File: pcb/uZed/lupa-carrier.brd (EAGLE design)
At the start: 99.7 x 57.1 mm, 93 parts, among them K1 694108105102

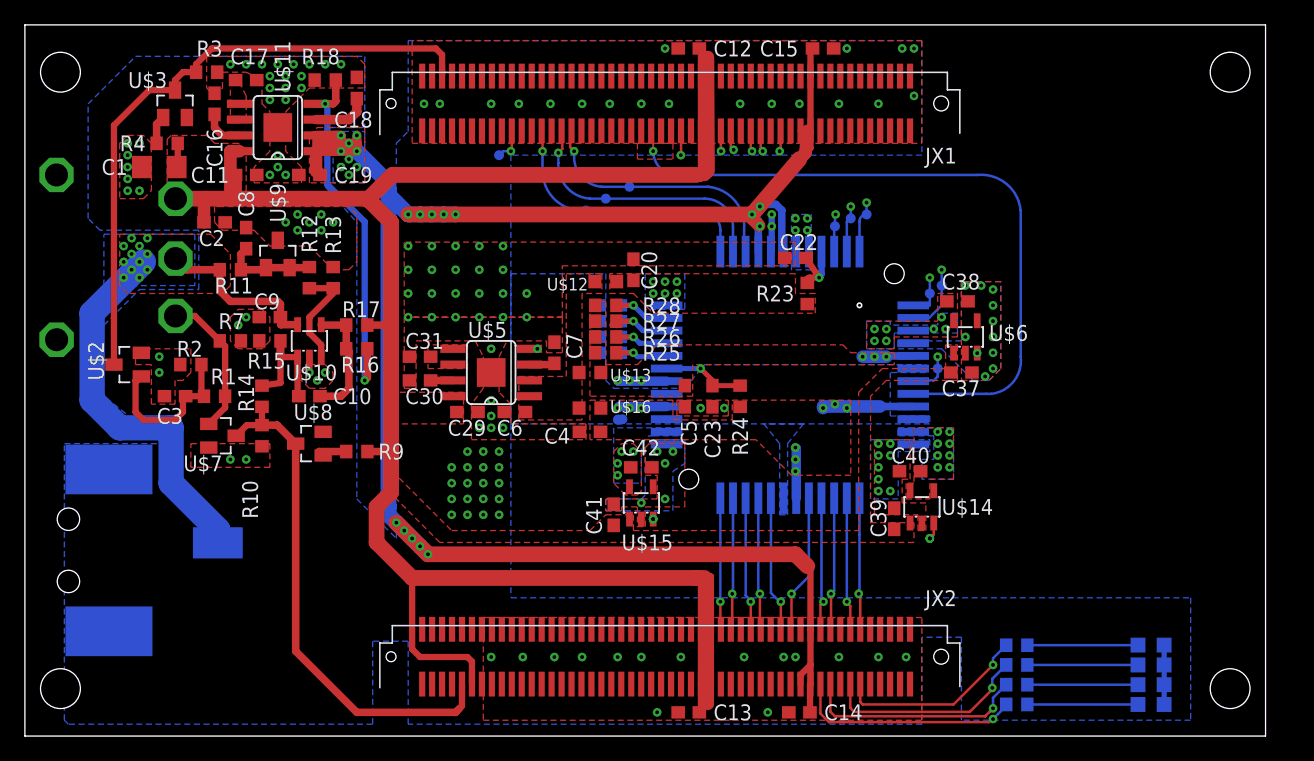
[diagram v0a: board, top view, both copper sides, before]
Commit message: added hdmi connectors, routing in progress
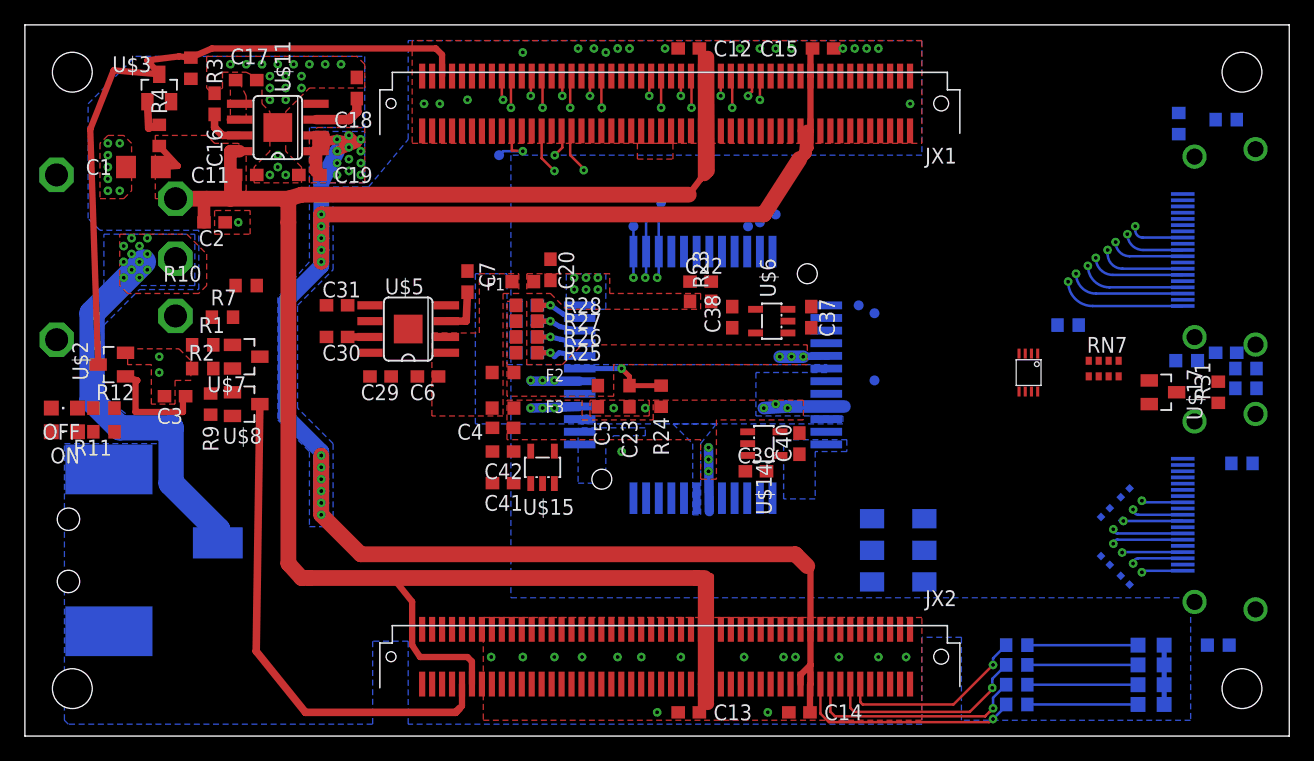
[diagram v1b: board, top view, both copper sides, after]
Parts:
- removed C10, C8, C9: .1uF, rcl:C0603
- removed R13, R14: 1k, rcl:R0603
- removed R15: 3k74, rcl:R0603
- removed R16: 0, rcl:R0603
- removed R17: 3k, rcl:R0603
- removed R18: 100k, rcl:R0603
- removed U$10: AP331A, lupa300-components:SOT25
- removed U$12, U$13, U$16: BLM18, lupa300-components:C0603K
- removed U$9: TL431A, lupa300-components:SOT23
- added C21, C28: .1uF, rcl:C0603K
- added C32: (no value), rcl:C0603
- added F1, F2, F3: BLM18, lupa300-components:C0603K
- added J5, J6: HDMI-TYPE-A-RECEPTICALFCI10029449, saanlima:FCI-HDMI-TYPE-A-RECEPT
- added OFF, ON: (no value), adafruit:CHIPLED_0805
- added PCA9306: PCA9306, saanlima:PSOP-8
- added R21, R8: 100K, rcl:R0603
- added R22, R32: 0, rcl:R0603
- added R29, R30, R31: 10K, rcl:R0603
- added RN3, RN4, RN5, RN6: 51, resistor-dil:EXB34V
- added RN7: 2k, resistor-dil:0603-ARV
- added U$17: BSS138, lupa300-components:SOT23
- added U$18: SI514, lupa300-components:XTAL-6PIN
- R12: value 1k5 -> 1k
- moved R12 19.6 mm to (6.35, 26.4), turned to 0 degrees
- moved C38 18.1 mm to (56.8, 33.7), turned to 90 degrees
- moved R11 16.5 mm to (6.35, 24.4), turned to 180 degrees
- moved U$6 15.6 mm to (60.0, 33.3), turned to 90 degrees
- moved U$14 13.7 mm to (59.4, 23.5), turned to 270 degrees
- moved C37 12.9 mm to (63.2, 33.7), turned to 90 degrees
- moved R9 12.3 mm to (14.9, 26.7), turned to 270 degrees
- moved R10 12.1 mm to (17.8, 36.2), turned to 180 degrees
- moved C39 11.7 mm to (58.7, 21.3), turned to 0 degrees
- moved C42 11.2 mm to (38.4, 22.9), turned to 180 degrees
- moved C41 9.25 mm to (38.4, 20.3), turned to 180 degrees
- moved C40 9.16 mm to (62.2, 23.5), turned to 270 degrees
- moved C7 9.03 mm to (35.6, 36.5)
- moved R23 8.60 mm to (54.3, 34.9), turned to 180 degrees
- moved U$15 8.44 mm to (41.6, 21.6)
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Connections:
- removed net 2V5_REF: C8.1, R11.2, R12.1, U$9.1, U$9.2
- removed net N$7: C10.1, R14.2, R15.1, U$10.1
- removed net N$9: C10.2, R16.1, R17.1, U$10.4
- removed net VADJ_EN: R16.2, R18.2, U$11.4
- new net 3V3: C32.1, PCA9306.2, R22.2, R31.1, RN7.1, RN7.2, U$18.P$6
- new net DET_CONTROL: R31.2, U$17.1
- new net HDMI_OSC: JX2.P$47, U$18.P$4
- new net HDMI_PU: R22.1, RN3.3, RN3.4, RN4.3, RN4.4, RN5.3, RN5.4, RN6.3, RN6.4
- new net N$17: J5.19, R29.2
- new net N$18: J6.19, R30.1, U$17.3
- new net N$19: J6.16, PCA9306.5, RN7.5
- new net N$20: J6.15, PCA9306.6, RN7.6
- new net N$21: J5.18, R32.2
- new net N$24: OFF.A, R12.1
- new net N$34: C21.1, J6.SH1, J6.SH2, J6.SH3, J6.SH4, R8.2
- new net N$6: C28.1, J5.SH1, J5.SH2, J5.SH3, J5.SH4, R21.2
- new net P1_CLOCK+: J6.10, JX1.P$66, RN3.2
- new net P1_CLOCK-: J6.12, JX1.P$64, RN3.1
- new net P1_DATA0+: J6.7, JX1.P$72, RN4.2
- new net P1_DATA0-: J6.9, JX1.P$70, RN4.1
- new net P1_DATA1+: J6.4, JX1.P$78, RN5.2
- new net P1_DATA1-: J6.6, JX1.P$76, RN5.1
- new net P1_DATA2+: J6.1, JX1.P$84, RN6.2
- new net P1_DATA2-: J6.3, JX1.P$82, RN6.1
- new net P2_CLOCK+: J5.10, JX1.P$34
- new net P2_CLOCK-: J5.12, JX1.P$32
- new net P2_DATA0+: J5.7, JX1.P$40
- new net P2_DATA0-: J5.9, JX1.P$38
- new net P2_DATA1+: J5.4, JX1.P$48
- new net P2_DATA1-: J5.6, JX1.P$46
- new net P2_DATA2+: J5.1, JX1.P$54
- new net P2_DATA2-: J5.3, JX1.P$52
- new net SCL2: PCA9306.3, RN7.8
- new net SCLC: U$18.P$2
- new net SDA2: PCA9306.4, RN7.7
- new net SDAC: U$18.P$1
- net 5V: now also J6.18, PCA9306.7, PCA9306.8, R11.1, R30.2, R32.1, RN7.3, RN7.4; no longer R17.2
- net 5V_OFF: now also R12.2
- net GND: now also C21.2, C28.2, C32.2, J5.11, J5.14, J5.17, J5.2, J5.5, J5.8, J6.11, J6.14, J6.17, J6.2, J6.5, J6.8, OFF.C, ON.C, PCA9306.1, R21.1, R29.1, R8.1, U$17.2, U$18.P$3; no longer C8.2, C9.2, R13.1, R15.2, R18.1, U$10.2, U$9.3
- net N$2: now also F1.2, F2.2, F3.2; no longer U$12.2, U$13.2, U$16.2
- net N$5: now also ON.A, R11.2; no longer R12.2, R13.2, U$10.3
- net VADC: now also F3.1; no longer U$16.1
- net VCCIO_EN: now also U$11.4; no longer R14.1
- net VDDA: now also F2.1; no longer U$13.1
- net VIN: no longer C9.1, R11.1, U$10.5
- net VPIX: now also F1.1; no longer U$12.1
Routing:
- net LPOWEN: track 89.6 -> 4.49 mm, vias 7 -> 1
- net P1_DATA2+: track 0.00 -> 84.7 mm, vias 0 -> 2
- net P1_DATA2-: track 0.00 -> 84.2 mm, vias 0 -> 2
- net P1_DATA1+: track 0.00 -> 81.3 mm, vias 0 -> 2
- net P1_DATA1-: track 0.00 -> 80.5 mm, vias 0 -> 2
- net P1_DATA0+: track 0.00 -> 78.2 mm, vias 0 -> 2
- net P1_DATA0-: track 0.00 -> 77.6 mm, vias 0 -> 2
- net P1_CLOCK+: track 0.00 -> 75.3 mm, vias 0 -> 2
- net P1_CLOCK-: track 0.00 -> 74.1 mm, vias 0 -> 2
- net P2_DATA2+: track 0.00 -> 57.5 mm, vias 0 -> 2
- net P2_DATA2-: track 0.00 -> 55.5 mm, vias 0 -> 2
- net CLK: track 55.1 -> 0.23 mm, vias 1 -> 0
- net P2_DATA1+: track 0.00 -> 51.6 mm, vias 0 -> 2
- net P2_DATA1-: track 0.00 -> 50.3 mm, vias 0 -> 2
- net P2_DATA0+: track 0.00 -> 47.3 mm, vias 0 -> 2
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- removed copper zone on layer 1, net N$23
- removed copper zone on layer 1, net VDDD
- removed copper zone on layer 16, net VDDD
- removed copper zone on layer 1, net VDDD1
- removed copper zone on layer 1, net VDDO
- removed copper zone on layer 16, net VDDO
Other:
- board size 99.7 x 57.1 mm -> 101.6 x 57.1 mm

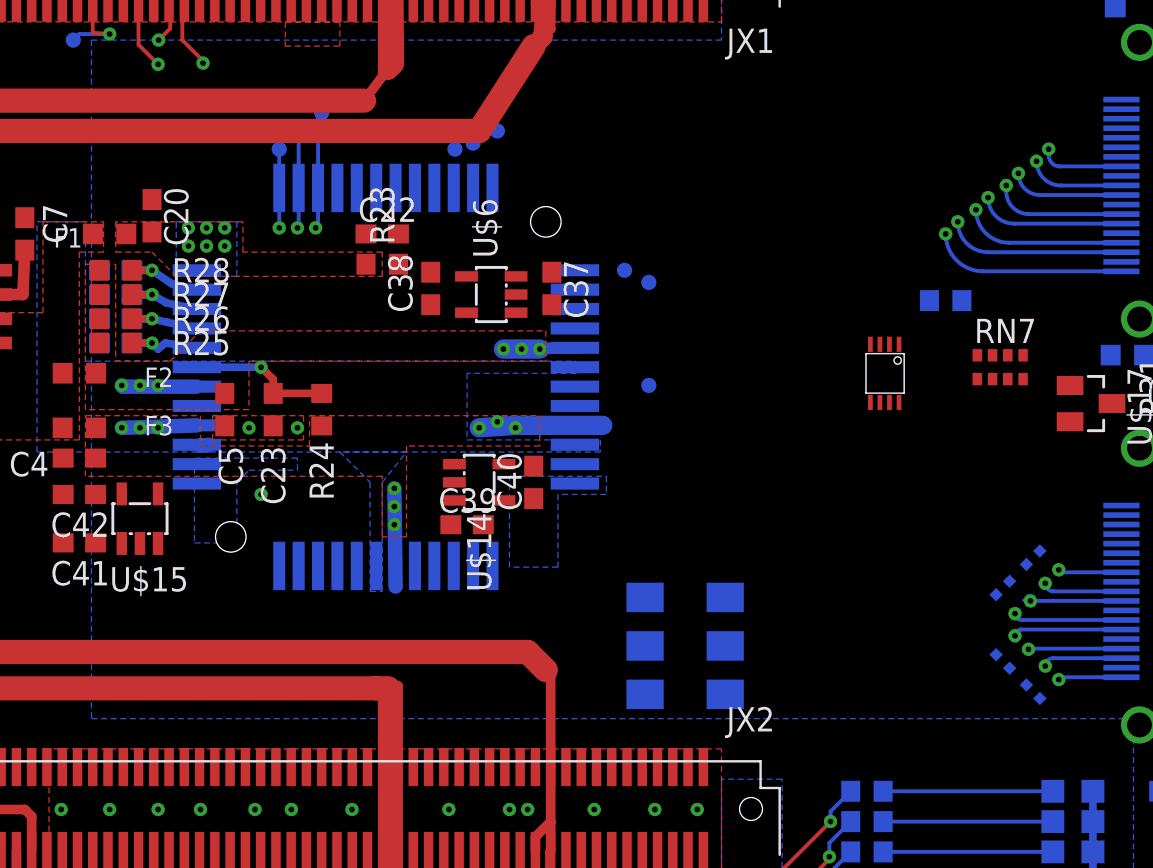
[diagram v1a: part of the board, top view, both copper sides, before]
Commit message: length tuned hdmi in traces
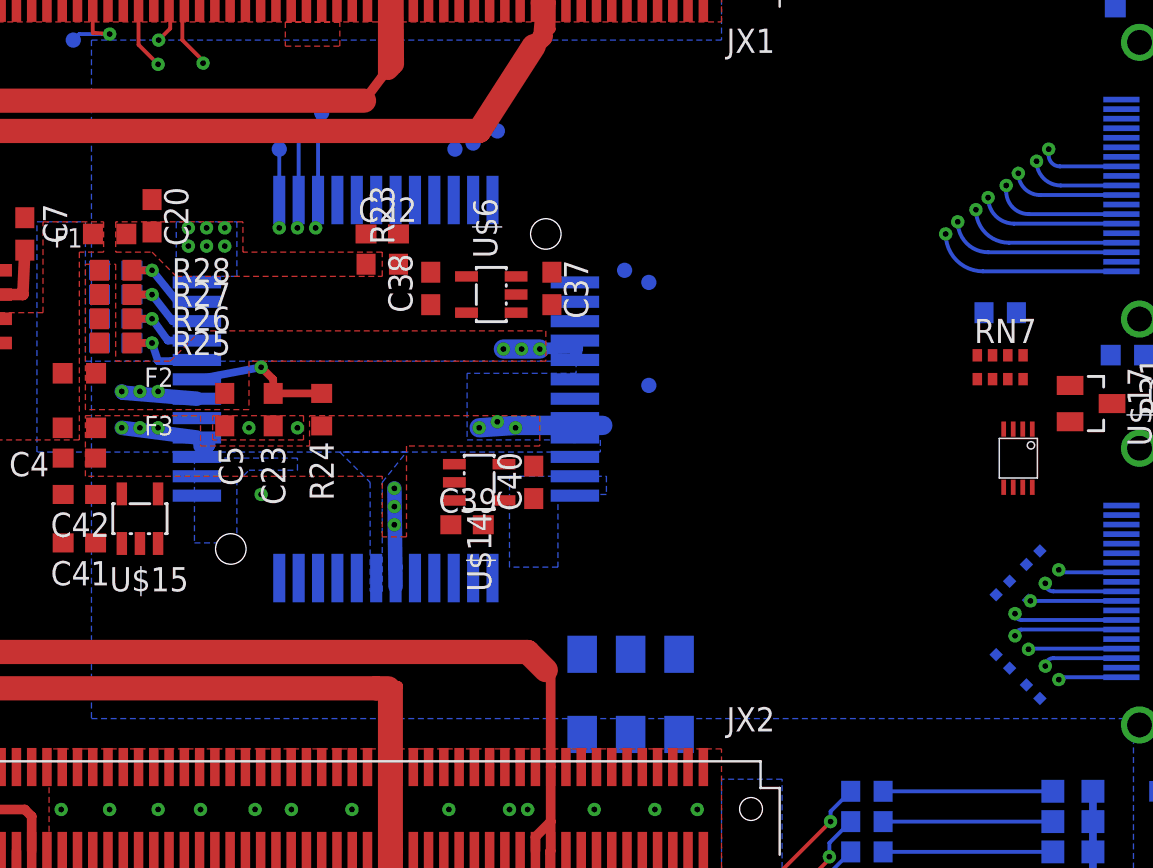
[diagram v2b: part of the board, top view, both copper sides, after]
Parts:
- moved PCA9306 8.28 mm to (87.6, 24.8)
- moved U$18 3.82 mm to (67.3, 12.4), turned to 90 degrees
- moved R22 2.93 mm to (86.7, 32.4)
- moved U$4 0.63 mm to (61.6, 21.3)
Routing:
- net P1_CLOCK-: track 74.1 -> 85.0 mm
- net P1_CLOCK+: track 75.3 -> 85.0 mm
- net P1_DATA0-: track 77.6 -> 84.6 mm
- net P1_DATA0+: track 78.2 -> 84.3 mm
- net P1_DATA1-: track 80.5 -> 84.1 mm
- net P1_DATA1+: track 81.3 -> 84.2 mm
- net VADC: track 17.2 -> 19.0 mm
- net P1_DATA2+: track 84.7 -> 85.4 mm
- net P1_DATA2-: track 84.2 -> 84.9 mm
- net BIAS1: track 4.71 -> 5.25 mm
- net VDDA: track 9.87 -> 10.4 mm
- net BIAS3: track 4.51 -> 5.04 mm
- net BIAS2: track 5.34 -> 5.87 mm

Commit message: length tuning
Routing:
- net P2_CLOCK-: track 45.4 -> 48.5 mm
- net P2_CLOCK+: track 47.2 -> 50.3 mm
- net P2_DATA0-: track 45.5 -> 48.2 mm
- net P2_DATA0+: track 47.3 -> 49.9 mm
- net P2_DATA2-: track 55.5 -> 58.1 mm
- net P2_DATA2+: track 57.5 -> 59.4 mm
- net P2_DATA1-: track 50.3 -> 51.9 mm
- net P2_DATA1+: track 51.6 -> 53.0 mm

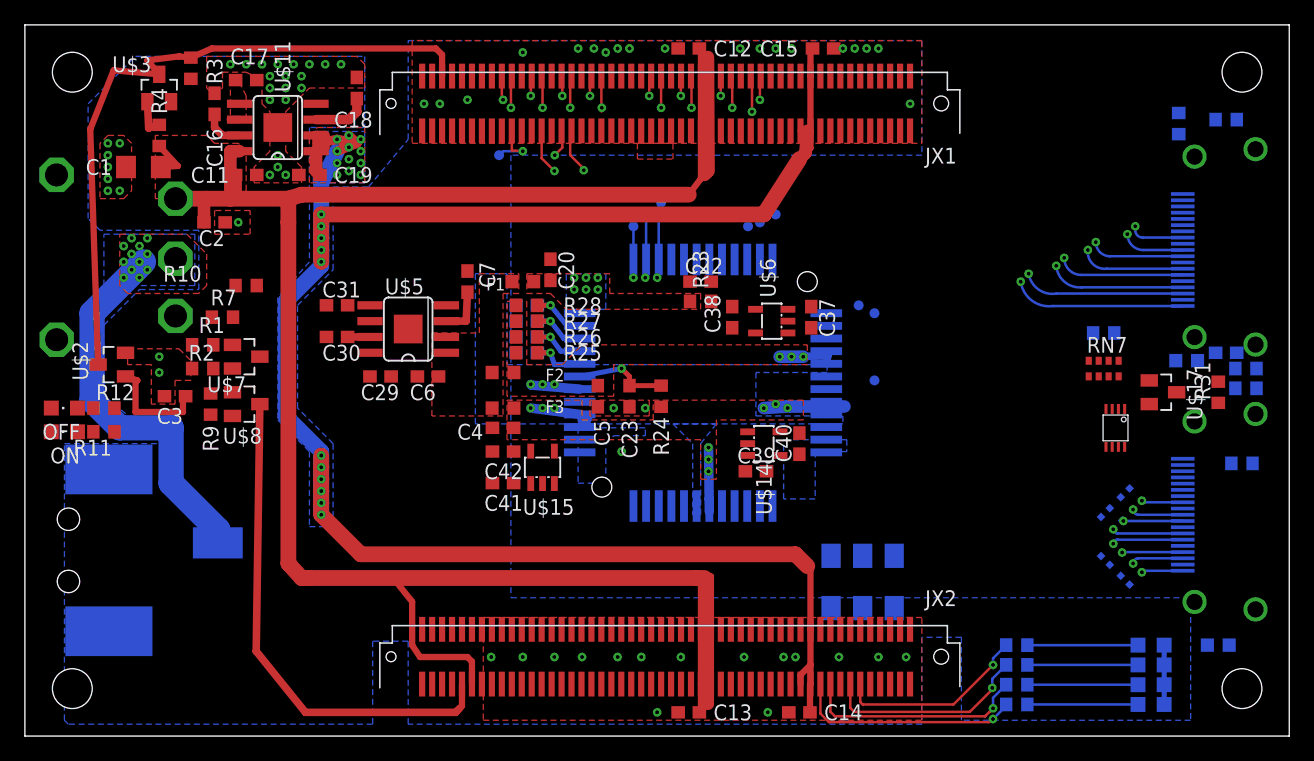
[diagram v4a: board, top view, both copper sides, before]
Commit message: beginning 4 layer hdmi board, discarded 6 layer approach
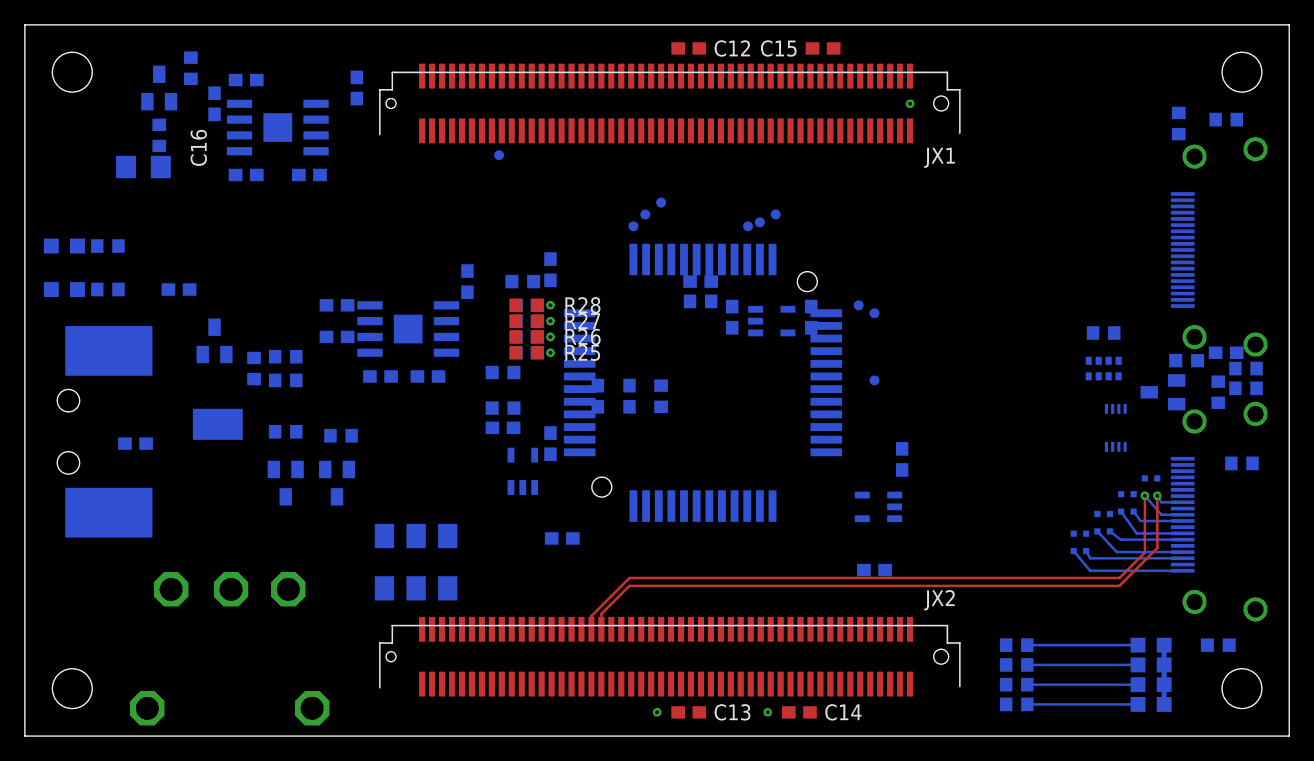
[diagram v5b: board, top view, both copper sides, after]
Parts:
- moved U$18 35.9 mm to (31.4, 14.0), turned to 270 degrees
- moved U$1 33.1 mm to (8.57, 13.7), turned to 180 degrees
- moved R12 13.0 mm to (6.67, 39.4), flipped to the bottom, turned to 180 degrees
- moved OFF 13.0 mm to (3.17, 39.4), flipped to the bottom, turned to 270 degrees
- moved C39 12.4 mm to (68.3, 13.3), flipped to the bottom
- moved R10 12.2 mm to (21.0, 24.4), flipped to the bottom
- moved R11 11.4 mm to (6.67, 35.9), flipped to the bottom, turned to 0 degrees
- moved ON 11.4 mm to (3.17, 35.9), flipped to the bottom, turned to 270 degrees
- moved R9 10.8 mm to (25.4, 24.1), flipped to the bottom, turned to 180 degrees
- moved U$7 10.6 mm to (21.0, 20.3), flipped to the bottom, turned to 180 degrees
- moved U$14 10.5 mm to (68.6, 18.4), flipped to the bottom
- moved U$8 9.68 mm to (25.1, 20.3), flipped to the bottom, turned to 180 degrees
- moved K1 9.53 mm to (0.00, 24.4)
- moved U$2 8.47 mm to (15.2, 31.8), flipped to the bottom, turned to 0 degrees
- moved C40 8.35 mm to (70.5, 22.2), flipped to the bottom
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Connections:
- net P1_CLOCK+: now also JX2.P$66
- net P1_CLOCK-: now also JX2.P$64
- net P1_DATA0+: now also JX2.P$72
- net P1_DATA0-: now also JX2.P$70
- net P1_DATA1+: now also JX2.P$78
- net P1_DATA1-: now also JX2.P$76
- net P1_DATA2+: now also JX2.P$84
- net P1_DATA2-: now also JX2.P$82
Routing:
- net 5V: track 200.5 -> 0.00 mm
- net VCCIO: track 162.2 -> 0.00 mm, vias 23 -> 0
- net P1_DATA0-: track 84.6 -> 4.32 mm, vias 2 -> 0
- net P1_DATA0+: track 84.3 -> 5.85 mm, vias 2 -> 0
- net P1_DATA1-: track 84.1 -> 6.08 mm, vias 2 -> 0
- net P1_DATA2-: track 84.9 -> 8.09 mm, vias 2 -> 0
- net P1_DATA1+: track 84.2 -> 7.57 mm, vias 2 -> 0
- net P1_DATA2+: track 85.4 -> 9.49 mm, vias 2 -> 0
- net P2_DATA2+: track 59.4 -> 0.00 mm, vias 2 -> 0
- net P2_DATA2-: track 58.1 -> 0.00 mm, vias 2 -> 0
- net PWR_EN: track 54.9 -> 0.00 mm
- net P2_DATA1+: track 53.0 -> 0.00 mm, vias 2 -> 0
- net P2_DATA1-: track 51.9 -> 0.00 mm, vias 2 -> 0
- net P2_CLOCK+: track 50.3 -> 0.00 mm, vias 2 -> 0
- net P2_DATA0+: track 49.9 -> 0.00 mm, vias 2 -> 0
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- removed copper zone on layer 1, net 5V
- removed copper zone on layer 1, net GND
- removed copper zone on layer 15, net GND
- removed copper zone on layer 16, net GND
- removed copper zone on layer 1, net N$11
- removed copper zone on layer 1, net N$2
- removed copper zone on layer 1, net VADC
- removed copper zone on layer 1, net VCCIO
- removed copper zone on layer 16, net VCCIO
- removed copper zone on layer 1, net VDDA
- removed copper zone on layer 16, net VDDD1
- removed copper zone on layer 1, net VIN
- removed copper zone on layer 16, net VIN
- removed copper zone on layer 1, net VPIX
- removed copper zone on layer 16, net VPIX
